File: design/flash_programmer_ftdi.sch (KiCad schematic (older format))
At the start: 13 parts, among them P2 USB_B, U7 FT230X

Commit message: Redo PCB: fix errors and shrink
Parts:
- P2: footprint Connect:USB_B -> Connectors:USB_B
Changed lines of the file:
@@
 EESchema Schematic File Version 2
-LIBS:atmega328p_tqfn
-LIBS:gls27sf010
-LIBS:max662a
-LIBS:2n3904
-LIBS:2n3906
-LIBS:ft232rl
-LIBS:ft230x
-LIBS:debug_pad
+LIBS:flash_programmer
 LIBS:power
 LIBS:device
@@
 $EndDescr
 $Comp
-L VCC #PWR041
+L VCC #PWR039
 U 1 1 58666138
 P 2500 1700
-F 0 "#PWR041" H 2500 1550 50  0001 C CNN
+F 0 "#PWR039" H 2500 1550 50  0001 C CNN
 F 1 "VCC" H 2500 1850 50  0000 C CNN
 F 2 "" H 2500 1700 50  0000 C CNN
@@
 $EndComp
 $Comp
-L GND #PWR042
+L GND #PWR040
 U 1 1 58666150
 P 1750 1000
-F 0 "#PWR042" H 1750 750 50  0001 C CNN
+F 0 "#PWR040" H 1750 750 50  0001 C CNN
 F 1 "GND" H 1750 850 50  0000 C CNN
 F 2 "" H 1750 1000 50  0000 C CNN
@@
 	1650 3400 1800 3400
 $Comp
-L GND #PWR043
+L GND #PWR041
 U 1 1 58666A15
 P 2400 3600
-F 0 "#PWR043" H 2400 3350 50  0001 C CNN
+F 0 "#PWR041" H 2400 3350 50  0001 C CNN
 F 1 "GND" H 2400 3450 50  0000 C CNN
 F 2 "" H 2400 3600 50  0000 C CNN
@@
 $EndComp
 $Comp
-L VCC #PWR044
+L VCC #PWR042
 U 1 1 58666A32
 P 1500 3600
-F 0 "#PWR044" H 1500 3450 50  0001 C CNN
+F 0 "#PWR042" H 1500 3450 50  0001 C CNN
 F 1 "VCC" H 1500 3750 50  0000 C CNN
 F 2 "" H 1500 3600 50  0000 C CNN
@@
 $EndComp
 $Comp
-L GND #PWR045
+L GND #PWR043
 U 1 1 58667B03
 P 4850 3050
-F 0 "#PWR045" H 4850 2800 50  0001 C CNN
+F 0 "#PWR043" H 4850 2800 50  0001 C CNN
 F 1 "GND" H 4850 2900 50  0000 C CNN
 F 2 "" H 4850 3050 50  0000 C CNN
@@
 	2300 1700 2500 1700
 $Comp
-L GND #PWR046
+L GND #PWR044
 U 1 1 58669DB0
 P 1750 2350
-F 0 "#PWR046" H 1750 2100 50  0001 C CNN
+F 0 "#PWR044" H 1750 2100 50  0001 C CNN
 F 1 "GND" H 1750 2200 50  0000 C CNN
 F 2 "" H 1750 2350 50  0000 C CNN
@@
 	4750 1550 4750 1450
 $Comp
-L VCC #PWR047
+L VCC #PWR045
 U 1 1 5867040E
 P 4750 1450
-F 0 "#PWR047" H 4750 1300 50  0001 C CNN
+F 0 "#PWR045" H 4750 1300 50  0001 C CNN
 F 1 "VCC" H 4750 1600 50  0000 C CNN
 F 2 "" H 4750 1450 50  0000 C CNN
@@
 	4000 1000 4000 750
 $Comp
-L GND #PWR048
+L GND #PWR046
 U 1 1 58670F4A
 P 4000 750
-F 0 "#PWR048" H 4000 500 50  0001 C CNN
+F 0 "#PWR046" H 4000 500 50  0001 C CNN
 F 1 "GND" H 4000 600 50  0000 C CNN
 F 2 "" H 4000 750 50  0000 C CNN
@@
 Connection ~ 2650 2850
 $Comp
-L GND #PWR049
+L GND #PWR047
 U 1 1 58674AD8
 P 2650 2950
-F 0 "#PWR049" H 2650 2700 50  0001 C CNN
+F 0 "#PWR047" H 2650 2700 50  0001 C CNN
 F 1 "GND" H 2650 2800 50  0000 C CNN
 F 2 "" H 2650 2950 50  0000 C CNN
@@
 	5650 1350 6000 1350
 $Comp
-L VCC #PWR050
+L VCC #PWR048
 U 1 1 5867D289
 P 5650 1350
-F 0 "#PWR050" H 5650 1200 50  0001 C CNN
+F 0 "#PWR048" H 5650 1200 50  0001 C CNN
 F 1 "VCC" H 5650 1500 50  0000 C CNN
 F 2 "" H 5650 1350 50  0000 C CNN
@@
 $EndComp
 $Comp
-L GND #PWR051
+L GND #PWR049
 U 1 1 5867D436
 P 5650 1550
-F 0 "#PWR051" H 5650 1300 50  0001 C CNN
+F 0 "#PWR049" H 5650 1300 50  0001 C CNN
 F 1 "GND" H 5650 1400 50  0000 C CNN
 F 2 "" H 5650 1550 50  0000 C CNN
@@
 GND
 $Comp
-L VCC #PWR052
+L VCC #PWR050
 U 1 1 5868E582
 P 7000 2400
-F 0 "#PWR052" H 7000 2250 50  0001 C CNN
+F 0 "#PWR050" H 7000 2250 50  0001 C CNN
 F 1 "VCC" H 7000 2550 50  0000 C CNN
 F 2 "" H 7000 2400 50  0000 C CNN
@@
 F 0 "P2" H 1400 2050 50  0000 C CNN
 F 1 "USB_B" H 1150 2450 50  0000 C CNN
-F 2 "Connect:USB_B" V 1150 2150 50  0001 C CNN
+F 2 "Connectors:USB_B" V 1150 2150 50  0001 C CNN
 F 3 "" V 1150 2150 50  0000 C CNN
 	1    1200 2250
@@
 $EndComp
 $Comp
-L GND #PWR053
+L GND #PWR051
 U 1 1 588E2AB4
 P 1100 2550
-F 0 "#PWR053" H 1100 2300 50  0001 C CNN
+F 0 "#PWR051" H 1100 2300 50  0001 C CNN
 F 1 "GND" H 1100 2400 50  0000 C CNN
 F 2 "" H 1100 2550 50  0000 C CNN

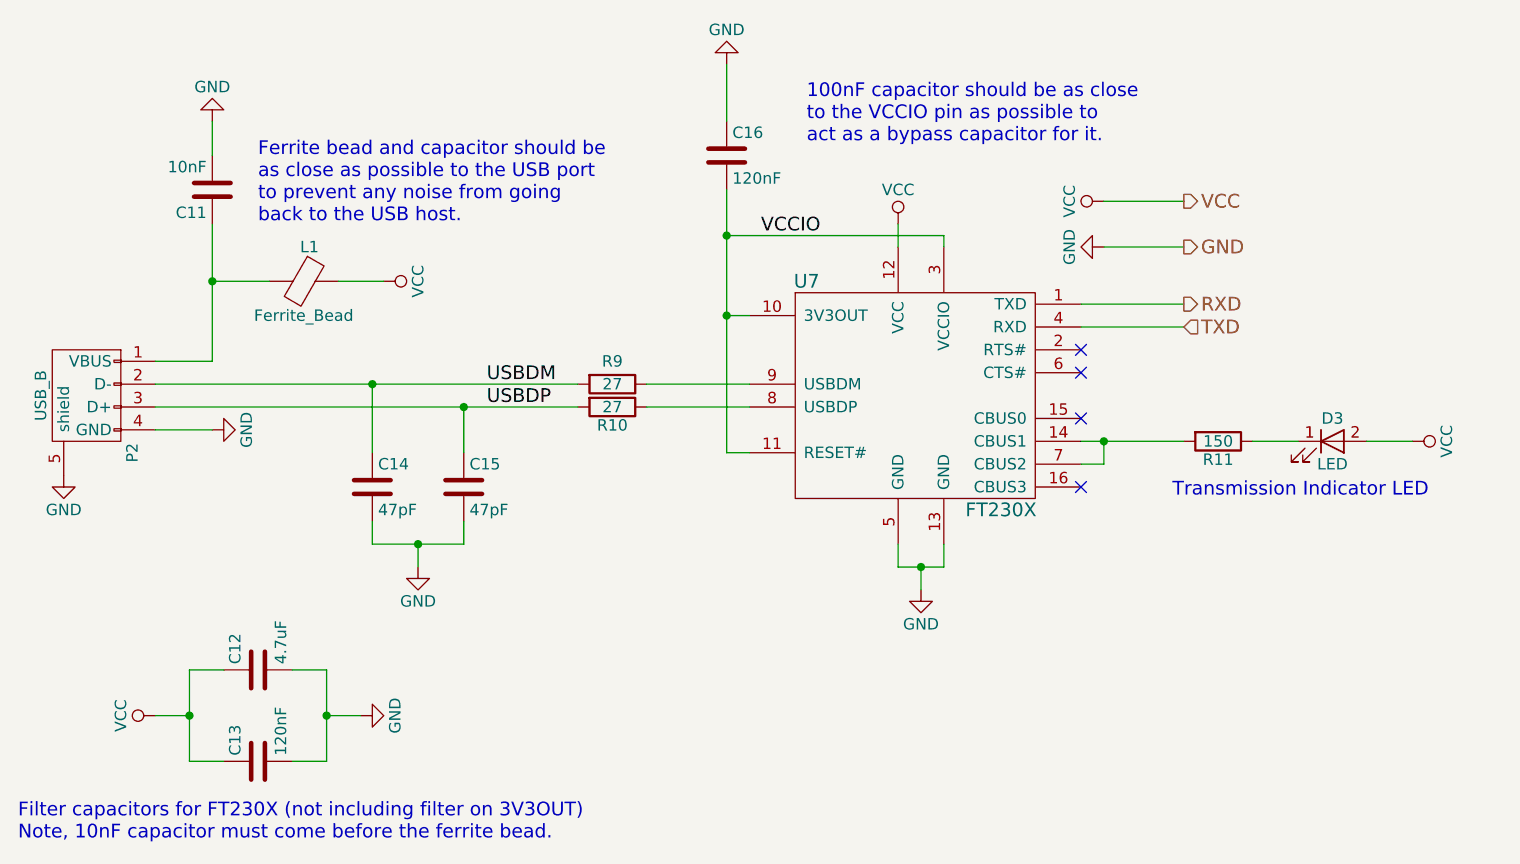
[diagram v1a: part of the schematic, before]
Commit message: Redo the A9_P circuit with a P-channel MOSFET to avoid voltage drop
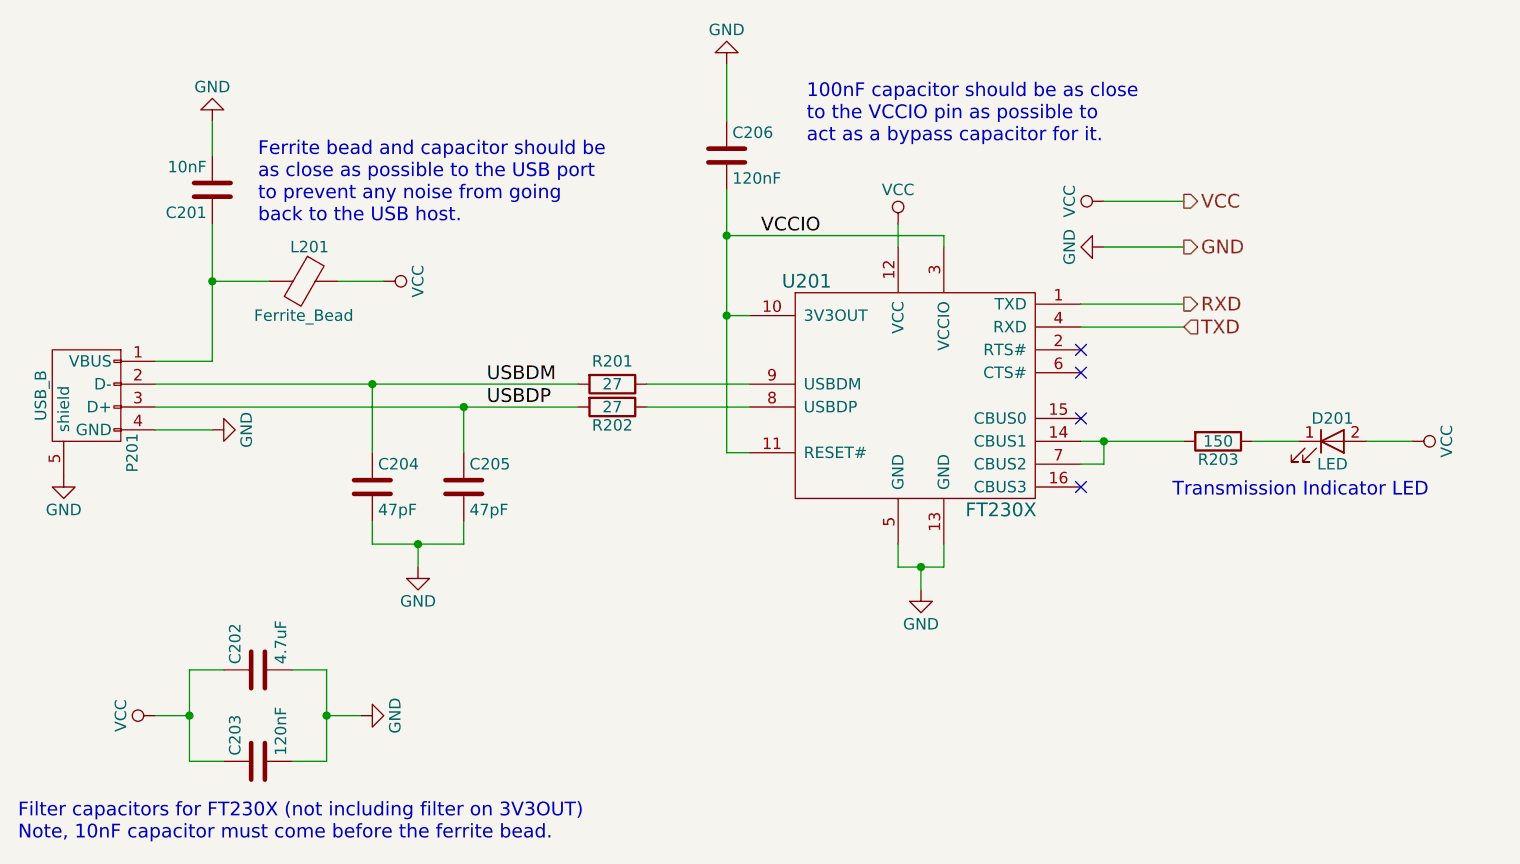
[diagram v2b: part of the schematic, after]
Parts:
- renumbered C11 to C201, C12 to C202, C13 to C203, C14 to C204, C15 to C205, C16 to C206, D3 to D201, L1 to L201, P2 to P201, R9 to R201, R10 to R202, R11 to R203, U7 to U201
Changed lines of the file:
@@
 $EndDescr
 $Comp
-L VCC #PWR039
+L VCC #PWR028
 U 1 1 58666138
 P 2500 1700
-F 0 "#PWR039" H 2500 1550 50  0001 C CNN
+F 0 "#PWR028" H 2500 1550 50  0001 C CNN
 F 1 "VCC" H 2500 1850 50  0000 C CNN
 F 2 "" H 2500 1700 50  0000 C CNN
@@
 $EndComp
 $Comp
-L GND #PWR040
+L GND #PWR029
 U 1 1 58666150
 P 1750 1000
-F 0 "#PWR040" H 1750 750 50  0001 C CNN
+F 0 "#PWR029" H 1750 750 50  0001 C CNN
 F 1 "GND" H 1750 850 50  0000 C CNN
 F 2 "" H 1750 1000 50  0000 C CNN
@@
 $EndComp
 $Comp
-L C C11
+L C C201
 U 1 1 58666168
 P 1750 1300
-F 0 "C11" H 1775 1400 50  0000 L CNN
+F 0 "C201" H 1775 1400 50  0000 L CNN
 F 1 "10nF" H 1775 1200 50  0000 L CNN
 F 2 "Capacitors_SMD:C_0805_HandSoldering" H 1788 1150 50  0001 C CNN
@@
 $EndComp
 $Comp
-L C C13
+L C C203
 U 1 1 586661BE
 P 1950 3800
-F 0 "C13" H 1975 3900 50  0000 L CNN
+F 0 "C203" H 1975 3900 50  0000 L CNN
 F 1 "120nF" H 1975 3700 50  0000 L CNN
 F 2 "Capacitors_SMD:C_0805_HandSoldering" H 1988 3650 50  0001 C CNN
@@
 $EndComp
 $Comp
-L C C12
+L C C202
 U 1 1 586661F4
 P 1950 3400
-F 0 "C12" H 1975 3500 50  0000 L CNN
+F 0 "C202" H 1975 3500 50  0000 L CNN
 F 1 "4.7uF" H 1975 3300 50  0000 L CNN
 F 2 "Capacitors_SMD:C_0805_HandSoldering" H 1988 3250 50  0001 C CNN
@@
 $EndComp
 $Comp
-L C C16
+L C C206
 U 1 1 5866621B
 P 4000 1150
-F 0 "C16" H 4025 1250 50  0000 L CNN
+F 0 "C206" H 4025 1250 50  0000 L CNN
 F 1 "120nF" H 4025 1050 50  0000 L CNN
 F 2 "Capacitors_SMD:C_0805_HandSoldering" H 4038 1000 50  0001 C CNN
@@
 	1650 3400 1800 3400
 $Comp
-L GND #PWR041
+L GND #PWR030
 U 1 1 58666A15
 P 2400 3600
-F 0 "#PWR041" H 2400 3350 50  0001 C CNN
+F 0 "#PWR030" H 2400 3350 50  0001 C CNN
 F 1 "GND" H 2400 3450 50  0000 C CNN
 F 2 "" H 2400 3600 50  0000 C CNN
@@
 $EndComp
 $Comp
-L VCC #PWR042
+L VCC #PWR031
 U 1 1 58666A32
 P 1500 3600
-F 0 "#PWR042" H 1500 3450 50  0001 C CNN
+F 0 "#PWR031" H 1500 3450 50  0001 C CNN
 F 1 "VCC" H 1500 3750 50  0000 C CNN
 F 2 "" H 1500 3600 50  0000 C CNN
@@
 $EndComp
 $Comp
-L GND #PWR043
+L GND #PWR032
 U 1 1 58667B03
 P 4850 3050
-F 0 "#PWR043" H 4850 2800 50  0001 C CNN
+F 0 "#PWR032" H 4850 2800 50  0001 C CNN
 F 1 "GND" H 4850 2900 50  0000 C CNN
 F 2 "" H 4850 3050 50  0000 C CNN
@@
 $EndComp
 $Comp
-L Ferrite_Bead L1
+L Ferrite_Bead L201
 U 1 1 58669A8D
 P 2150 1700
-F 0 "L1" V 2000 1725 50  0000 C CNN
+F 0 "L201" V 2000 1725 50  0000 C CNN
 F 1 "Ferrite_Bead" V 2300 1700 50  0000 C CNN
 F 2 "Capacitors_SMD:C_0805_HandSoldering" V 2080 1700 50  0001 C CNN
@@
 	2300 1700 2500 1700
 $Comp
-L GND #PWR044
+L GND #PWR033
 U 1 1 58669DB0
 P 1750 2350
-F 0 "#PWR044" H 1750 2100 50  0001 C CNN
+F 0 "#PWR033" H 1750 2100 50  0001 C CNN
 F 1 "GND" H 1750 2200 50  0000 C CNN
 F 2 "" H 1750 2350 50  0000 C CNN
@@
 Filter capacitors for FT230X (not including filter on 3V3OUT)\nNote, 10nF capacitor must come before the ferrite bead.
 $Comp
-L LED D3
+L LED D201
 U 1 1 5866C67B
 P 6650 2400
-F 0 "D3" H 6650 2500 50  0000 C CNN
+F 0 "D201" H 6650 2500 50  0000 C CNN
 F 1 "LED" H 6650 2300 50  0000 C CNN
 F 2 "LEDs:LED_0805" H 6650 2400 50  0001 C CNN
@@
 Transmission Indicator LED
 $Comp
-L FT230X U7
+L FT230X U201
 U 1 1 5866F07F
 P 4850 2650
-F 0 "U7" H 4350 3600 60  0000 C CNN
+F 0 "U201" H 4350 3600 60  0000 C CNN
 F 1 "FT230X" H 5200 2600 60  0000 C CNN
 F 2 "ssop-16:SSOP-16" H 4850 2650 60  0001 C CNN
@@
 	4750 1550 4750 1450
 $Comp
-L VCC #PWR045
+L VCC #PWR034
 U 1 1 5867040E
 P 4750 1450
-F 0 "#PWR045" H 4750 1300 50  0001 C CNN
+F 0 "#PWR034" H 4750 1300 50  0001 C CNN
 F 1 "VCC" H 4750 1600 50  0000 C CNN
 F 2 "" H 4750 1450 50  0000 C CNN
@@
 	4000 1000 4000 750
 $Comp
-L GND #PWR046
+L GND #PWR035
 U 1 1 58670F4A
 P 4000 750
-F 0 "#PWR046" H 4000 500 50  0001 C CNN
+F 0 "#PWR035" H 4000 500 50  0001 C CNN
 F 1 "GND" H 4000 600 50  0000 C CNN
 F 2 "" H 4000 750 50  0000 C CNN
@@
 	5550 1900 6000 1900
 $Comp
-L R R10
+L R R202
 U 1 1 58674423
 P 3500 2250
-F 0 "R10" V 3580 2250 50  0000 C CNN
+F 0 "R202" V 3580 2250 50  0000 C CNN
 F 1 "27" V 3500 2250 50  0000 C CNN
 F 2 "Resistors_SMD:R_0805_HandSoldering" V 3430 2250 50  0001 C CNN
@@
 $EndComp
 $Comp
-L R R9
+L R R201
 U 1 1 586744C9
 P 3500 2150
-F 0 "R9" V 3400 2150 50  0000 C CNN
+F 0 "R201" V 3400 2150 50  0000 C CNN
 F 1 "27" V 3500 2150 50  0000 C CNN
 F 2 "Resistors_SMD:R_0805_HandSoldering" V 3430 2150 50  0001 C CNN
@@
 	4100 2250 3650 2250
 $Comp
-L C C14
+L C C204
 U 1 1 5867487B
 P 2450 2600
-F 0 "C14" H 2475 2700 50  0000 L CNN
+F 0 "C204" H 2475 2700 50  0000 L CNN
 F 1 "47pF" H 2475 2500 50  0000 L CNN
 F 2 "Capacitors_SMD:C_0805_HandSoldering" H 2488 2450 50  0001 C CNN
@@
 $EndComp
 $Comp
-L C C15
+L C C205
 U 1 1 58674901
 P 2850 2600
-F 0 "C15" H 2875 2700 50  0000 L CNN
+F 0 "C205" H 2875 2700 50  0000 L CNN
 F 1 "47pF" H 2875 2500 50  0000 L CNN
 F 2 "Capacitors_SMD:C_0805_HandSoldering" H 2888 2450 50  0001 C CNN
@@
 Connection ~ 2650 2850
 $Comp
-L GND #PWR047
+L GND #PWR036
 U 1 1 58674AD8
 P 2650 2950
-F 0 "#PWR047" H 2650 2700 50  0001 C CNN
+F 0 "#PWR036" H 2650 2700 50  0001 C CNN
 F 1 "GND" H 2650 2800 50  0000 C CNN
 F 2 "" H 2650 2950 50  0000 C CNN
@@
 100nF capacitor should be as close\nto the VCCIO pin as possible to \nact as a bypass capacitor for it.
 $Comp
-L R R11
+L R R203
 U 1 1 58678751
 P 6150 2400
-F 0 "R11" V 6230 2400 50  0000 C CNN
+F 0 "R203" V 6230 2400 50  0000 C CNN
 F 1 "150" V 6150 2400 50  0000 C CNN
 F 2 "Resistors_SMD:R_0805_HandSoldering" V 6080 2400 50  0001 C CNN
@@
 	5650 1350 6000 1350
 $Comp
-L VCC #PWR048
+L VCC #PWR037
 U 1 1 5867D289
 P 5650 1350
-F 0 "#PWR048" H 5650 1200 50  0001 C CNN
+F 0 "#PWR037" H 5650 1200 50  0001 C CNN
 F 1 "VCC" H 5650 1500 50  0000 C CNN
 F 2 "" H 5650 1350 50  0000 C CNN
@@
 $EndComp
 $Comp
-L GND #PWR049
+L GND #PWR038
 U 1 1 5867D436
 P 5650 1550
-F 0 "#PWR049" H 5650 1300 50  0001 C CNN
+F 0 "#PWR038" H 5650 1300 50  0001 C CNN
 F 1 "GND" H 5650 1400 50  0000 C CNN
 F 2 "" H 5650 1550 50  0000 C CNN
@@
 GND
 $Comp
-L VCC #PWR050
+L VCC #PWR039
 U 1 1 5868E582
 P 7000 2400
-F 0 "#PWR050" H 7000 2250 50  0001 C CNN
+F 0 "#PWR039" H 7000 2250 50  0001 C CNN
 F 1 "VCC" H 7000 2550 50  0000 C CNN
 F 2 "" H 7000 2400 50  0000 C CNN
@@
 VCCIO
 $Comp
-L USB_B P2
+L USB_B P201
 U 1 1 5866CC44
 P 1200 2250
-F 0 "P2" H 1400 2050 50  0000 C CNN
+F 0 "P201" H 1400 2050 50  0000 C CNN
 F 1 "USB_B" H 1150 2450 50  0000 C CNN
 F 2 "Connectors:USB_B" V 1150 2150 50  0001 C CNN
@@
 $EndComp
 $Comp
-L GND #PWR051
+L GND #PWR040
 U 1 1 588E2AB4
 P 1100 2550
-F 0 "#PWR051" H 1100 2300 50  0001 C CNN
+F 0 "#PWR040" H 1100 2300 50  0001 C CNN
 F 1 "GND" H 1100 2400 50  0000 C CNN
 F 2 "" H 1100 2550 50  0000 C CNN
